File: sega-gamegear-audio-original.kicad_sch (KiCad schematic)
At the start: 20 parts, among them CN1 292161-6, CN2 CONN 2P, IC1 TDA2822D, J1 CONN MINI JACK

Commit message: update gitignore
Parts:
- R1, R2: Manufacturer_Part_Number RT0603BRD07100RL -> RT0603BRD0756KL
- R3, R4: Manufacturer_Part_Number RT0603BRD07100RL -> RT0603BRD074R7L
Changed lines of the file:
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@@
       (effects (font (size 1.27 1.27)) hide)
     )
-    (property "Manufacturer_Part_Number" "RT0603BRD07100RL" (at 173.99 96.52 90)
+    (property "Manufacturer_Part_Number" "RT0603BRD074R7L" (at 173.99 96.52 90)
       (effects (font (size 1.27 1.27)) (justify right))
     )
@@
       (effects (font (size 1.27 1.27)) hide)
     )
-    (property "Manufacturer_Part_Number" "RT0603BRD07100RL" (at 68.58 80.01 0)
+    (property "Manufacturer_Part_Number" "RT0603BRD0756KL" (at 68.58 80.01 0)
       (effects (font (size 1.27 1.27)))
     )
@@
       (effects (font (size 1.27 1.27)) hide)
     )
-    (property "Manufacturer_Part_Number" "RT0603BRD07100RL" (at 68.58 95.25 0)
+    (property "Manufacturer_Part_Number" "RT0603BRD0756KL" (at 68.58 95.25 0)
       (effects (font (size 1.27 1.27)))
     )
@@
       (effects (font (size 1.27 1.27)) hide)
     )
-    (property "Manufacturer_Part_Number" "RT0603BRD07100RL" (at 173.99 121.92 90)
-      (effects (font (size 1.27 1.27)) (justify right))
-    )
+    (property "Manufacturer_Part_Number" "RT0603BRD074R7L" (at 173.99 121.92 90)
+      (effects (font (size 1.27 1.27)) (justify right))
+    )

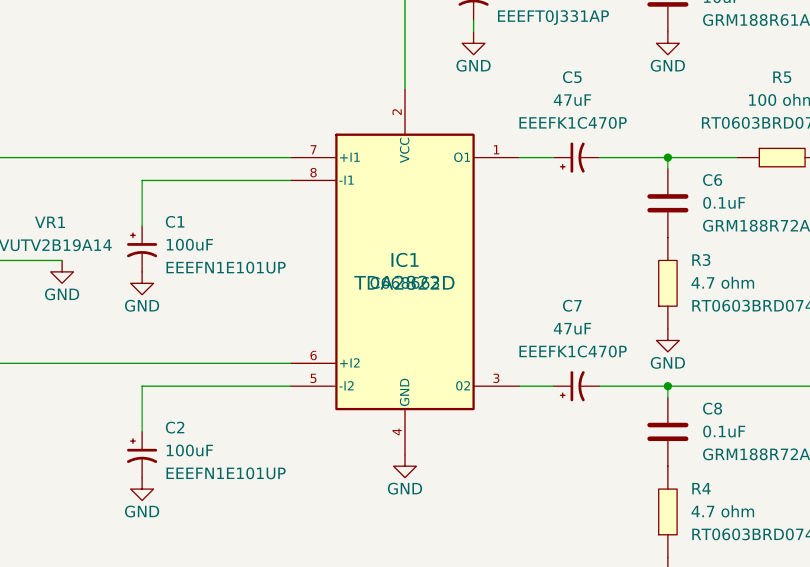
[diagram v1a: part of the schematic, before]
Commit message: fix symbol spelling mistake
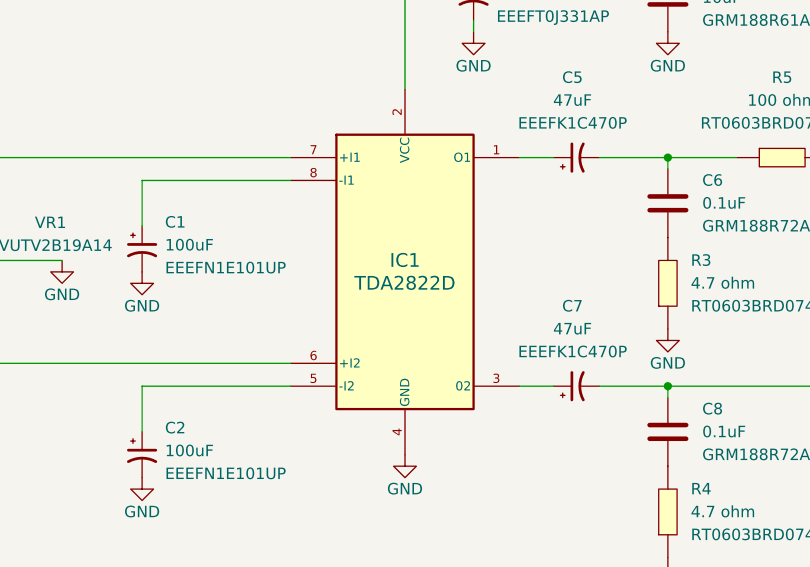
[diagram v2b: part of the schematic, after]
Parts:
- IC1: symbol TDA2882D:TDA2822D -> TDA2822D:TDA2822D
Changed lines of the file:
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@@
     )
   )
-  (symbol (lib_id "TDA2882D:TDA2822D") (at 142.24 93.98 0) (unit 1)
+  (symbol (lib_id "TDA2822D:TDA2822D") (at 142.24 93.98 0) (unit 1)
     (in_bom yes) (on_board yes) (dnp no)
     (property "Reference" "IC1" (at 142.24 91.44 0)
@@
       (effects (font (size 1.524 1.524)))
     )
-    (property "Footprint" "Sega GameGear Audio Board Original:TDA2822D" (at 142.24 105.41 0)
+    (property "Footprint" "Sega GameGear Audio Board Original:TDA2822D" (at 142.24 123.19 0)
       (effects (font (size 1.27 1.27)) hide)
     )
@@
       (effects (font (size 1.27 1.27)) hide)
     )
-    (property "LCSC Part" "C668663" (at 142.24 93.98 0)
-      (effects (font (size 1.27 1.27)))
+    (property "LCSC Part" "C668663" (at 142.24 120.65 0)
+      (effects (font (size 1.27 1.27)) hide)
     )
     (pin "4")

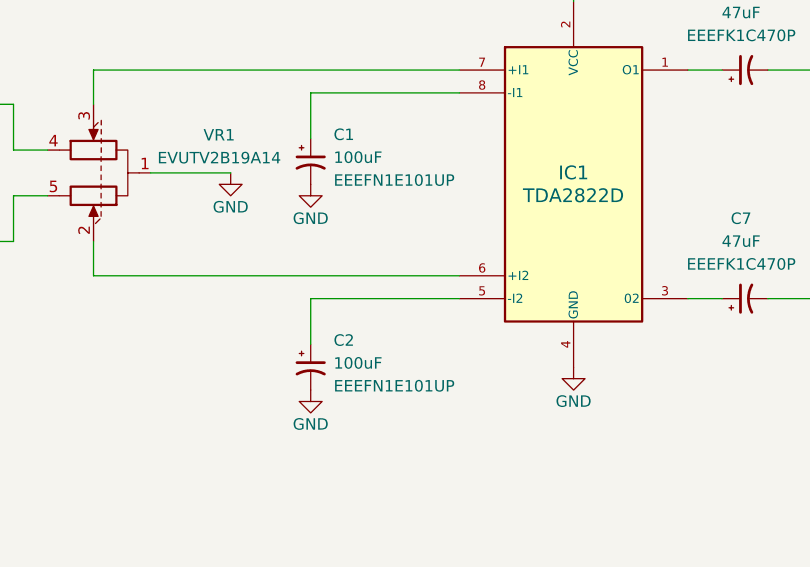
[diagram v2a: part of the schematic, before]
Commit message: swap out 100uf cap with legacy version for now
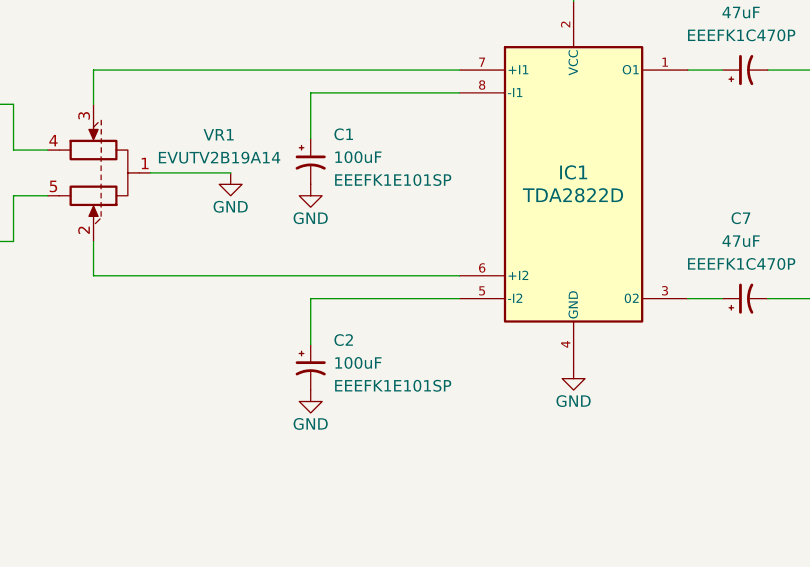
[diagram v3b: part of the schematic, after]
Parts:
- C1, C2: symbol EEEFN1E101UP:EEEFN1E101UP -> EEEFK1E101SP:EEEFK1E101SP; LCSC Part C494824 -> C178540; Manufacturer_Part_Number EEEFN1E101UP -> EEEFK1E101SP
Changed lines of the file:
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@@
     )
   )
-  (symbol (lib_id "EEEFN1E101UP:EEEFN1E101UP") (at 113.03 90.17 270) (unit 1)
+  (symbol (lib_id "EEEFK1E101SP:EEEFK1E101SP") (at 113.03 90.17 270) (unit 1)
     (in_bom yes) (on_board yes) (dnp no) (fields_autoplaced)
     (property "Reference" "C1" (at 115.57 87.1982 90)
@@
       (effects (font (size 1.27 1.27)) (justify left top) hide)
     )
-    (property "Manufacturer_Part_Number" "EEEFN1E101UP" (at 115.57 92.2782 90)
-      (effects (font (size 1.27 1.27)) (justify left))
-    )
-    (property "LCSC Part" "C494824" (at 113.03 90.17 0)
+    (property "Manufacturer_Part_Number" "EEEFK1E101SP" (at 115.57 92.2782 90)
+      (effects (font (size 1.27 1.27)) (justify left))
+    )
+    (property "LCSC Part" "C178540" (at 113.03 90.17 0)
       (effects (font (size 1.27 1.27)) hide)
     )
@@
     )
   )
-  (symbol (lib_id "EEEFN1E101UP:EEEFN1E101UP") (at 113.03 113.03 270) (unit 1)
+  (symbol (lib_id "EEEFK1E101SP:EEEFK1E101SP") (at 113.03 113.03 270) (unit 1)
     (in_bom yes) (on_board yes) (dnp no) (fields_autoplaced)
     (property "Reference" "C2" (at 115.57 110.0582 90)
@@
       (effects (font (size 1.27 1.27)) (justify left top) hide)
     )
-    (property "Manufacturer_Part_Number" "EEEFN1E101UP" (at 115.57 115.1382 90)
-      (effects (font (size 1.27 1.27)) (justify left))
-    )
-    (property "LCSC Part" "C494824" (at 113.03 113.03 0)
-      (effects (font (size 1.27 1.27)) hide)
-    )
+    (property "Manufacturer_Part_Number" "EEEFK1E101SP" (at 115.57 115.1382 90)
+      (effects (font (size 1.27 1.27)) (justify left))
+    )
+    (property "LCSC Part" "C178540" (at 113.03 113.03 0)
+      (effects (font (size 1.27 1.27)) hide)
+    )
